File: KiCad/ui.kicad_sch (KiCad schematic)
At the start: 40 parts, among them SW1 PEC11R-4215F-S0024, SW2 PEC11R-4215F-S0024, U10 SN74HC14PWR, U11 LM35DGS, U8 SN74AHCT244DBR, U9 24LC256-I_ST

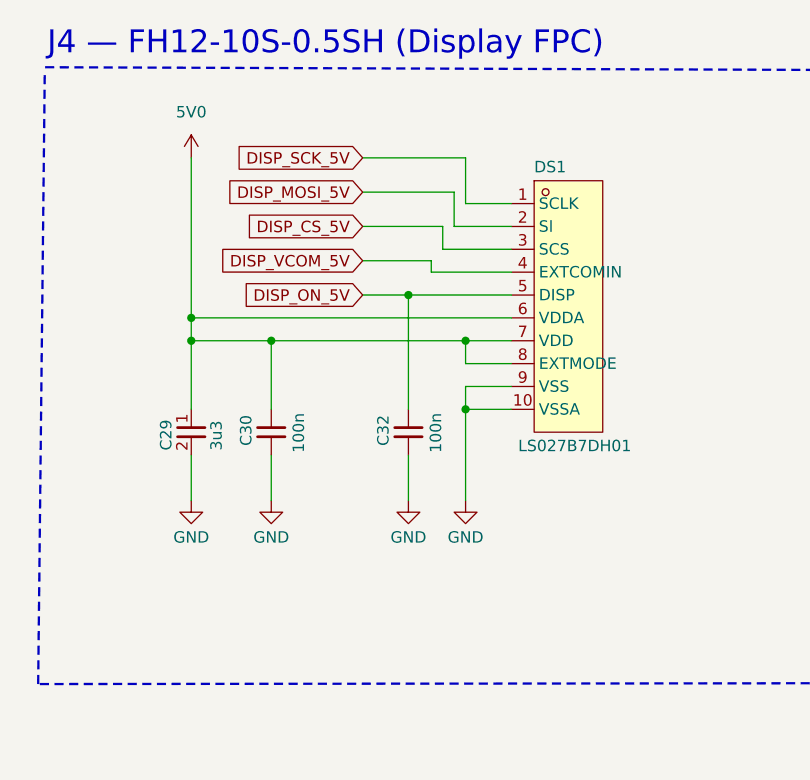
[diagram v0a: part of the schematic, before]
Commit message: Basic board layout changed. MCU pinout changed accordingly
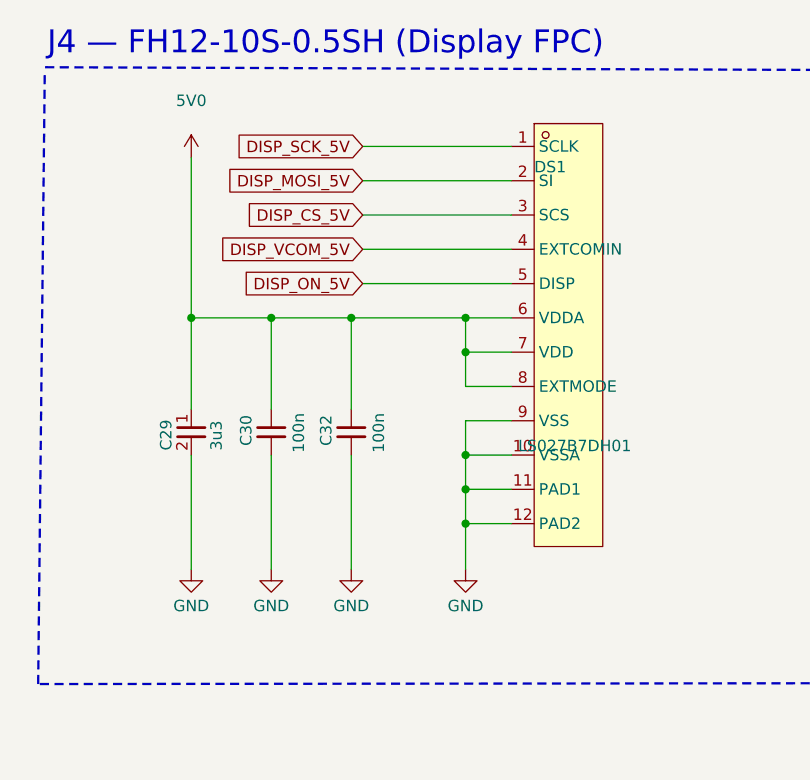
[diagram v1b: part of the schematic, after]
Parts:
- DS1: footprint sldrnrd:Header_FFC_1.5mm_10 -> sldrnrd:Display_LS027B7DH01
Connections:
- net 5V0: now also C32.1
- net DISP_ON_5V: no longer C32.1
- net GND: now also DS1.11 (PAD1), DS1.12 (PAD2)
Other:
- moved on the sheet: C32

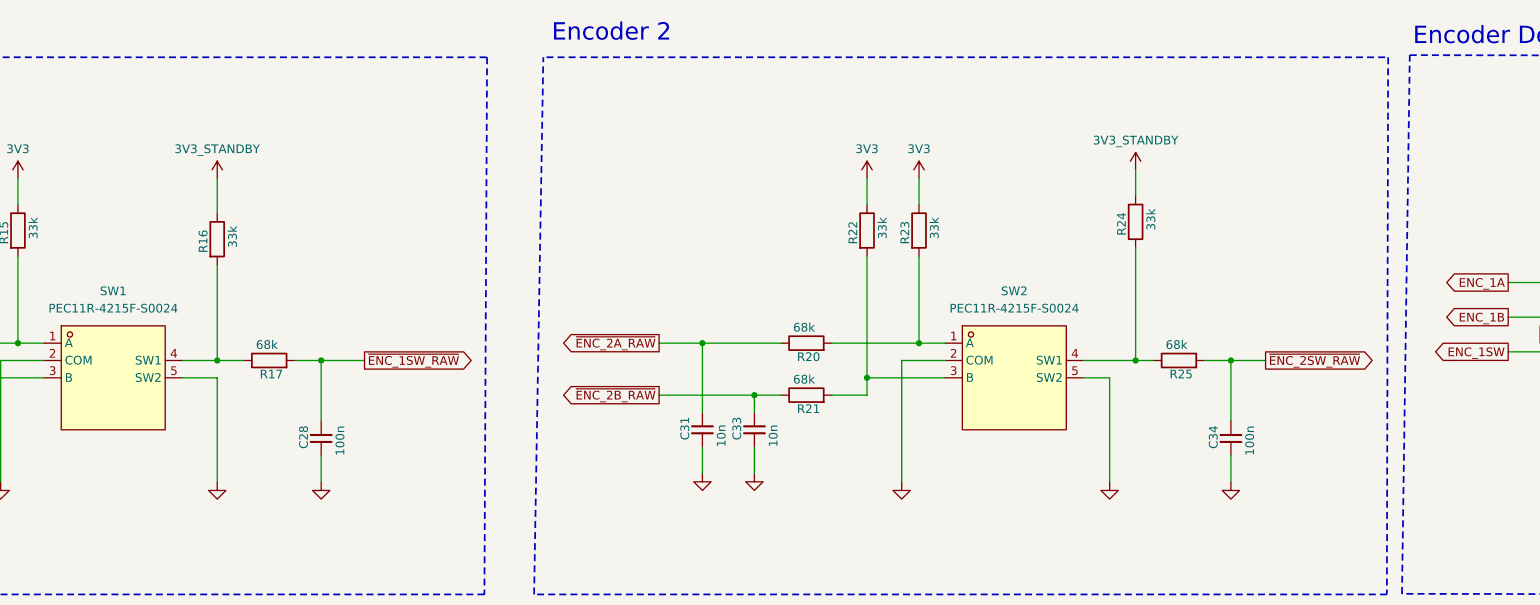
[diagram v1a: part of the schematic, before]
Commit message: Encoder fixed, main parts and dimensions locked
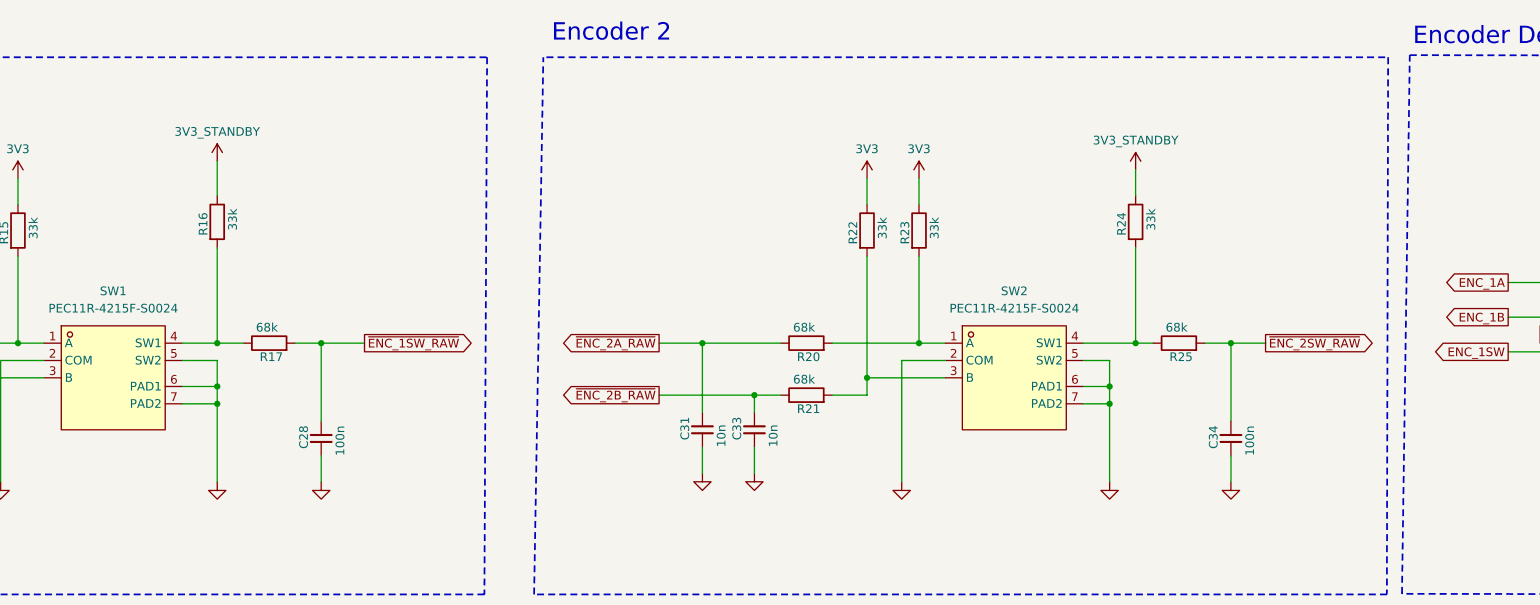
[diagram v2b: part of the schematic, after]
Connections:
- net GND: now also SW1.6 (PAD1), SW1.7 (PAD2), SW2.6 (PAD1), SW2.7 (PAD2)
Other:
- moved on the sheet: R16, R17, R25

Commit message: Board largely routed, except power and gnd
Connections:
- net 5V0: no longer C32.1
- net DISP_MOSI: now also U8.8 (1A4); no longer U8.4 (1A2)
- net DISP_MOSI_5V: now also U8.12 (1Y4); no longer U8.16 (1Y2)
- net DISP_ON: now also U8.2 (1A1); no longer U8.17 (2A4)
- net DISP_ON_5V: now also C32.1, U8.18 (1Y1); no longer U8.3 (2Y4)
- net DISP_SCK: now also U8.17 (2A4); no longer U8.2 (1A1)
- net DISP_SCK_5V: now also U8.3 (2Y4); no longer U8.18 (1Y1)
- net DISP_VCOM: now also U8.4 (1A2); no longer U8.8 (1A4)
- net DISP_VCOM_5V: now also U8.16 (1Y2); no longer U8.12 (1Y4)
- net ENC_1A: now also U10.4 (2Y); no longer U10.2 (1Y)
- net ENC_1B: now also U10.6 (3Y); no longer U10.4 (2Y)
- net ENC_1SW: now also U10.2 (1Y); no longer U10.6 (3Y)
- net GND: now also U8.10 (GND)
- net ~{ENC_1A_RAW}: now also U10.3 (2A); no longer U10.1 (1A)
- net ~{ENC_1B_RAW}: now also U10.5 (3A); no longer U10.3 (2A)
- net ~{ENC_1SW_RAW}: now also U10.1 (1A); no longer U10.5 (3A)
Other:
- moved on the sheet: C32

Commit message: Environmental sensor added, mostly routed.
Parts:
- added C42: 100n, sldrnrd:C_0603, symbol sldrnrd:Capacitor/C_0603
- added U12: BME280, sldrnrd:LGA-8_2.5x2.5mm_P0.65mm, symbol sldrnrd:Sensor/BME280
- BZ1: LCSC (none) -> C20181991; MPN (none) -> CPT-9019A-SMT-TR; Manufacturer (none) -> CUI
- D4: symbol sldrnrd:LED/LED_Green_0603 -> sldrnrd:LED/LED_Yellow_0603; LCSC C72043 -> C2287; MPN 19-217/GHC-YR1S2/3T -> KT-0603Y; Manufacturer EVERLIGHT -> KENTO
- R10, R11, R26: symbol sldrnrd:Resistor/R_0603 -> sldrnrd:Resistor/R0603_1k; LCSC (none) -> C21190; MPN (none) -> 0603WAF1001T5E; Manufacturer (none) -> Uni-Royal
- U10: LCSC (none) -> C6821; MPN (none) -> SN74HC14PWR; Manufacturer (none) -> TI
- U11: footprint sldrnrd:SOT-23 -> sldrnrd:SOT-23-3; LCSC (none) -> C9900081740
- U9: LCSC (none) -> C87823; MPN (none) -> 24LC256-I/ST; Manufacturer (none) -> Microchip
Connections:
- net 3V3: now also C42.1, U12.2 (CSB), U12.5 (SDO), U12.6 (VDDIO), U12.8 (VDD)
- net EEPROM_SCL: now also U12.4 (SCK)
- net EEPROM_SDA: now also U12.3 (SDI)
- net GND: now also C42.2, U12.1 (GND), U12.7 (GND)
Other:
- note added: "24LC256 EEPROM"
- note added: "Environmental sensor BME280"
- note removed: "24LC256 EEPROM (U9)"

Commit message: JST headers fixed, no more errors, fully routed
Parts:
- R18, R19: symbol sldrnrd:Resistor/R_0603 -> sldrnrd:Resistor/R0603_5k1; LCSC (none) -> C23186; MPN (none) -> 0603WAF5101T5E; Manufacturer (none) -> Uni-Royal
- renumbered C42 to C34, C34 to C35, C35 to C36, C36 to C37, U12 to U10, U10 to U11, U11 to U12

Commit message: Capacitors changed to specific symbols, board layout not yet complete
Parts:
- C26, C27, C28, C30, C32, C34, C35, C36, C37: symbol sldrnrd:Capacitor/C_0603 -> sldrnrd:Capacitor/C0603_100n; Dielectric (none) -> X7R; LCSC (none) -> C14663; MPN (none) -> CC0603KRX7R9BB104; Manufacturer (none) -> Yageo; Voltage (none) -> 50V
- C29: value 3u3 -> 2u2; symbol sldrnrd:Capacitor/C_0805 -> sldrnrd:Capacitor/C0805_2u2; Dielectric (none) -> X7R; LCSC (none) -> C126589; MPN (none) -> GCM21BR71C225KA64L; Manufacturer (none) -> Murata; Voltage (none) -> 16V
